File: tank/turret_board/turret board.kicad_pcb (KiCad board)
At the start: 2 copper layers, 69 x 39 mm, 22 parts, among them P1 Power, P2 IR Beacon, P3 SigIn, P4 IR Tx, P5 IR Rx, U1 LM317T, U2 pixart_ir, Y1 Crystal_4pin

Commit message: main board v0.1
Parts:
- removed ?: , Tank:MIAR
- removed P1: Power, JST:JST_EH_B02B-EH-A_02x2.50mm_Straight
- removed P2: IR Beacon, JST:JST_EH_B02B-EH-A_02x2.50mm_Straight
- removed P3: SigIn, JST:JST_EH_B04B-EH-A_04x2.50mm_Straight
- removed P4: IR Tx, JST:JST_EH_B02B-EH-A_02x2.50mm_Straight
- removed P5: IR Rx, JST:JST_EH_B03B-EH-A_03x2.50mm_Straight
- removed the REF** at (150.0, 70.0)
- removed the REF** at (209.0, 70.0)
- added Beacon1: CONN_01X02, JST:JST_EH_B02B-EH-A_02x2.50mm_Straight, F.Cu at (208.3, 64.8)
- added C5: C, Capacitors_THT:C_Disc_D3.0mm_W1.6mm_P2.50mm, F.Cu at (177.8, 86.4)
- added D1: D, Diodes_THT:D_T-1_P5.08mm_Horizontal, F.Cu at (181.6, 82.5)
- added D2: D, Diodes_THT:D_T-1_P5.08mm_Horizontal, F.Cu at (189.2, 82.5)
- added D3: D, Diodes_THT:D_T-1_P5.08mm_Horizontal, F.Cu at (185.4, 82.5)
- added G***: LOGO, modules:miar_logo, B.Cu at (182.9, 71.1)
- added J1: Conn_01x06, Connectors_JAE:JAE_LY20-06P-2T_2x03x2.00mm_Straight, F.Cu at (224.8, 96.5)
- added J2: Conn_01x06, Connectors_JAE:JAE_LY20-06P-2T_2x03x2.00mm_Straight, F.Cu at (232.4, 77.5)
- added Pwr1: CONN_01X02, JST:JST_EH_B02B-EH-A_02x2.50mm_Straight, F.Cu at (172.7, 76.2)
- added Q1: Q_NPN_BCE, Transistors_OldSowjetAera:OldSowjetaera_Transistor_Type-I_SmallPads, F.Cu at (184.2, 67.3)
- added Q2: Q_NPN_BCE, Transistors_OldSowjetAera:OldSowjetaera_Transistor_Type-I_SmallPads, F.Cu at (185.4, 92.7)
- added R8: R, Resistors_THT:R_Axial_DIN0207_L6.3mm_D2.5mm_P7.62mm_Horizontal, F.Cu at (218.4, 78.7)
- added R9: R, Resistors_THT:R_Axial_DIN0207_L6.3mm_D2.5mm_P7.62mm_Horizontal, F.Cu at (223.5, 78.7)
- added REF**: MountingHole_2.2mm_M2, Mounting_Holes:MountingHole_2.2mm_M2, F.Cu at (232.4, 72.4)
- added REF**: MountingHole_3.2mm_M3, Mounting_Holes:MountingHole_3.2mm_M3, F.Cu at (171.4, 66.0)
- added REF**: MountingHole_3.2mm_M3, Mounting_Holes:MountingHole_3.2mm_M3, F.Cu at (215.9, 94.0)
- added REF**: MountingHole_2.2mm_M2, Mounting_Holes:MountingHole_2.2mm_M2, F.Cu at (232.4, 88.9)
- added Rx1: CONN_01X03, JST:JST_EH_B03B-EH-A_03x2.50mm_Straight, F.Cu at (218.4, 64.8)
- added SigIn1: CONN_01X04, JST:JST_EH_B04B-EH-A_04x2.50mm_Straight, F.Cu at (172.7, 88.9)
- added Tx1: TX, JST:JST_EH_B02B-EH-A_02x2.50mm_Straight, F.Cu at (223.5, 83.8)
- U2: footprint pixart_ir -> modules:pixart_ir
- moved Y1 58.3 mm to (213.4, 72.4), turned to 270 degrees
- moved U2 54.0 mm to (238.8, 85.1), turned to 0 degrees
- moved U1 41.7 mm to (198.1, 94.0)
- moved R4 29.9 mm to (218.4, 81.3), turned to 270 degrees
- moved C3 29.8 mm to (194.3, 64.8), turned to 180 degrees
- moved R7 23.5 mm to (177.8, 90.2), turned to 270 degrees
- moved R1 22.6 mm to (193.0, 78.7), turned to 90 degrees
- moved C1 18.5 mm to (200.7, 64.8), turned to 180 degrees
- moved R3 17.8 mm to (200.7, 88.9)
- moved C4 16.7 mm to (185.4, 86.4)
- moved R2 16.2 mm to (193.0, 88.9)
- moved R5 15.5 mm to (196.8, 71.1), turned to 270 degrees
- moved C2 13.1 mm to (207.0, 94.0), turned to 0 degrees
- moved R6 10.5 mm to (196.8, 88.9), turned to 90 degrees
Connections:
- C1 pad 2: Net-(C1-Pad2) -> GND
- C2 pad 1: Net-(C1-Pad2) -> Net-(C1-Pad1)
- C2 pad 2: Net-(C1-Pad2) -> GND
- C3 pad 1: +3V3 -> 3.3V
- C3 pad 2: Net-(C1-Pad2) -> GND
- C4 pad 1: Net-(C4-Pad1) -> RESET
- C4 pad 2: Net-(C1-Pad2) -> GND
- R1 pad 2: Net-(C1-Pad1) -> IRSig
- R3 pad 2: Net-(C1-Pad2) -> GND
- R4 pad 1: +3V3 -> 3.3V
- R5 pad 1: +3V3 -> 3.3V
- R5 pad 2: Net-(C4-Pad1) -> RESET
- R6 pad 1: +3V3 -> SLC
- R6 pad 2: Net-(P3-Pad2) -> 3.3V
- R7 pad 1: +3V3 -> SDA
- R7 pad 2: Net-(P3-Pad1) -> 3.3V
- U1 pad 2: +3V3 -> 3.3V
- U1 pad 3: Net-(C1-Pad2) -> Net-(C1-Pad1)
- U2 pad 1: +3V3 -> Net-(J2-Pad1)
- U2 pad 2: Net-(C1-Pad2) -> Net-(J2-Pad2)
- U2 pad 3: Net-(C1-Pad2) -> Net-(J2-Pad2)
- U2 pad 5: Net-(P3-Pad1) -> Net-(J2-Pad6)
- U2 pad 6: Net-(P3-Pad2) -> Net-(J2-Pad5)
- U2 pad 7: Net-(U2-Pad7) -> Net-(J2-Pad4)
- U2 pad 8: Net-(C4-Pad1) -> Net-(J2-Pad3)
- Y1 pad 14: Net-(C1-Pad1) -> 5V
- Y1 pad 7: Net-(C1-Pad2) -> GND
- Y1 pad 8: Net-(U2-Pad7) -> Net-(J1-Pad4)
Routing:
- net GND: track 0.00 -> 151.4 mm, vias 0 -> 1
- net Net-(C1-Pad2): track 127.5 -> 0.00 mm
- net 3.3V: track 0.00 -> 100.7 mm
- net Net-(Rx1-Pad3): track 0.00 -> 81.3 mm, vias 0 -> 1
- net +3V3: track 75.7 -> 0.00 mm, vias 2 -> 0
- net Beacon: track 0.00 -> 75.6 mm
- net Net-(P3-Pad1): track 69.6 -> 0.00 mm, vias 1 -> 0
- net Net-(D2-Pad1): track 0.00 -> 65.2 mm, vias 0 -> 1
- net SLC: track 0.00 -> 60.5 mm, vias 0 -> 1
- net SDA: track 0.00 -> 57.7 mm, vias 0 -> 1
- net Net-(P3-Pad2): track 50.8 -> 0.00 mm, vias 2 -> 0
- net RESET: track 0.00 -> 50.7 mm, vias 0 -> 1
- net IRSig: track 0.00 -> 38.7 mm
- net Net-(C4-Pad1): track 38.0 -> 0.00 mm
- net Net-(J2-Pad3): track 0.00 -> 33.8 mm
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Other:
- board size 69 x 39 mm -> 80 x 44.4 mm
- board text added: "Turret Board v0.3 Laser Tag Robot Tank M.I.A.R. Labs nick.groesz@gmail.com"
- board text removed: "Turret Board v0.2 Laser Bot M.I.A.R. Labs"

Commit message: interim
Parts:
- removed C2, C4: C, Capacitors_THT:C_Disc_D3.0mm_W1.6mm_P2.50mm
- removed G***: LOGO, modules:miar_logo
- removed Pwr1: CONN_01X02, JST:JST_EH_B02B-EH-A_02x2.50mm_Straight
- removed R1, R3, R4: R, Resistors_THT:R_Axial_DIN0207_L6.3mm_D2.5mm_P7.62mm_Horizontal
- removed the REF** at (232.4, 72.4)
- removed the REF** at (171.4, 66.0)
- removed the REF** at (215.9, 94.0)
- removed the REF** at (232.4, 88.9)
- added J3: Conn_01x02_Male, JST:JST_EH_B02B-EH-A_02x2.50mm_Straight, F.Cu at (186.7, 117.5)
- added REF**: MountingHole_2.2mm_M2, Mounting_Holes:MountingHole_2.2mm_M2, F.Cu at (186.7, 96.5)
- added REF**: MountingHole_2.2mm_M2, Mounting_Holes:MountingHole_2.2mm_M2, F.Cu at (187.3, 123.2)
- added REF**: MountingHole_2.2mm_M2, Mounting_Holes:MountingHole_2.2mm_M2, F.Cu at (222.2, 96.5)
- added REF**: MountingHole_2.2mm_M2, Mounting_Holes:MountingHole_2.2mm_M2, F.Cu at (222.2, 123.2)
- J1, J2: footprint Connectors_JAE:JAE_LY20-06P-2T_2x03x2.00mm_Straight -> Pin_Headers:Pin_Header_Straight_2x03_Pitch2.54mm
- Q1, Q2: value Q_NPN_BCE -> 2N3904; footprint Transistors_OldSowjetAera:OldSowjetaera_Transistor_Type-I_SmallPads -> TO_SOT_Packages_THT:TO-92_Inline_Narrow_Oval
- U1: value LM317T -> KA378R33; footprint Tank:LM317T -> TO_SOT_Packages_THT:TO-220-4_Vertical
- moved C1 59.0 mm to (192.4, 123.2), turned to 90 degrees
- moved R5 57.5 mm to (218.4, 124.5), turned to 90 degrees
- moved Q1 56.8 mm to (209.6, 118.1)
- moved C3 52.1 mm to (192.4, 116.8), turned to 90 degrees
- moved R8 50.0 mm to (196.8, 123.8)
- moved R7 44.1 mm to (206.4, 123.8), turned to 90 degrees
- moved R9 42.6 mm to (203.2, 116.2), turned to 270 degrees
- moved R2 41.9 mm to (215.3, 124.5)
- moved Q2 39.4 mm to (209.6, 123.8), turned to 0 degrees
- moved C5 36.0 mm to (201.3, 113.7), turned to 180 degrees
- moved R6 35.1 mm to (200.0, 123.8)
- moved D1 34.3 mm to (200.7, 111.1)
- moved Y1 33.8 mm to (203.8, 104.8), turned to 0 degrees
- moved Rx1 33.5 mm to (207.6, 96.5), turned to 180 degrees
- moved Beacon1 31.6 mm to (214.0, 95.9)
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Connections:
- D2 pad 2: Net-(D2-Pad2) -> IRSig
- D3 pad 2: Net-(D2-Pad2) -> IRSig
- J1 pad 3: RESET -> GND
- Q1 pad 1: Net-(D3-Pad1) -> GND
- Q1 pad 2: Net-(D2-Pad1) -> Net-(D3-Pad1)
- Q1 pad 3: GND -> Net-(D2-Pad1)
- Q2 pad 1: Net-(Q2-Pad1) -> GND
- Q2 pad 2: Beacon -> Net-(Q2-Pad2)
- Q2 pad 3: GND -> Beacon
- R2 pad 1: Net-(Q2-Pad1) -> Net-(Q2-Pad2)
- R5 pad 2: RESET -> GND
- Rx1 pad 3: Net-(Rx1-Pad3) -> IRRx
- SigIn1 pad 3: Net-(Rx1-Pad3) -> IRSig
- SigIn1 pad 4: IRSig -> IRRx
- U1 pad 1: Net-(R3-Pad1) -> Net-(C1-Pad1)
- U1 pad 3: Net-(C1-Pad1) -> GND
- Y1 pad 14: 5V -> 3.3V
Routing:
- net GND: track 151.4 -> 0.00 mm, vias 1 -> 0
- net 3.3V: track 100.7 -> 0.00 mm
- net Net-(Rx1-Pad3): track 81.3 -> 0.00 mm, vias 1 -> 0
- net Beacon: track 75.6 -> 0.00 mm
- net Net-(C1-Pad1): track 73.5 -> 0.00 mm, vias 1 -> 0
- net Net-(D2-Pad1): track 65.2 -> 0.00 mm, vias 1 -> 0
- net SLC: track 60.5 -> 0.00 mm, vias 1 -> 0
- net SDA: track 57.7 -> 0.00 mm, vias 1 -> 0
- net RESET: track 50.7 -> 0.00 mm, vias 1 -> 0
- net IRSig: track 38.7 -> 0.00 mm
- net Net-(J2-Pad3): track 33.8 -> 0.00 mm
- net 5V: track 27.6 -> 0.00 mm
- net Net-(R3-Pad1): track 23.9 -> 0.00 mm
- net Net-(D3-Pad1): track 22.4 -> 0.00 mm
- net Net-(J2-Pad2): track 20.5 -> 0.00 mm
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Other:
- board size 80 x 44.4 mm -> 44.4 x 34.3 mm
- board text removed: "Turret Board v0.3 Laser Tag Robot Tank M.I.A.R. Labs nick.groesz@gmail.com"

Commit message: Turret Board v0.4
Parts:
- added G***: LOGO, modules:Tank, B.Cu at (211.5, 116.8)
- added REF**: MountingHole_2.2mm_M2, Mounting_Holes:MountingHole_2.2mm_M2, F.Cu at (241.3, 117.5)
- added REF**: MountingHole_2.2mm_M2, Mounting_Holes:MountingHole_2.2mm_M2, F.Cu at (231.8, 116.8)
- added REF**: MountingHole_2.2mm_M2, Mounting_Holes:MountingHole_2.2mm_M2, F.Cu at (231.8, 102.2)
- added REF**: MountingHole_2.2mm_M2, Mounting_Holes:MountingHole_2.2mm_M2, F.Cu at (241.3, 101.6)
- moved U1 26.4 mm to (207.6, 123.8)
- moved R7 20.7 mm to (192.4, 108.6)
- moved R8 15.4 mm to (198.8, 108.6)
- moved Q2 14.5 mm to (203.8, 110.5), turned to 90 degrees
- moved Q1 14.5 mm to (203.8, 104.8), turned to 90 degrees
- moved Y1 13.9 mm to (217.2, 101.0), turned to 270 degrees
- moved R9 10.8 mm to (195.6, 108.6), turned to 90 degrees
- moved D3 10.5 mm to (204.5, 113.7), turned to 270 degrees
- moved R6 9.53 mm to (192.4, 118.1)
- moved SigIn1 7.01 mm to (187.3, 101.6), turned to 270 degrees
- moved C1 6.48 mm to (198.8, 121.9), turned to 270 degrees
- moved R5 5.24 mm to (217.2, 119.4), turned to 0 degrees
- moved C3 5.12 mm to (193.0, 121.9), turned to 270 degrees
- moved R2 5.08 mm to (215.3, 119.4), turned to 180 degrees
- moved D1 4.58 mm to (196.8, 113.7), turned to 270 degrees
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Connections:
- C1 pad 1: Net-(C1-Pad1) -> 5V
- J1 pad 3: GND -> RESET
- J3 pad 1: Net-(C1-Pad1) -> 5V
- R5 pad 2: GND -> RESET
- U1 pad 1: Net-(C1-Pad1) -> 5V
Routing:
- net GND: track 0.00 -> 119.0 mm
- net 5V: track 0.00 -> 93.2 mm
- net 3.3V: track 0.00 -> 82.6 mm, vias 0 -> 1
- net SLC: track 0.00 -> 56.0 mm
- net SDA: track 0.00 -> 43.5 mm
- net IRRx: track 0.00 -> 34.3 mm
- net Beacon: track 0.00 -> 33.3 mm
- net IRSig: track 0.00 -> 29.9 mm
- net Net-(J2-Pad1): track 0.00 -> 22.1 mm
- net Net-(Q2-Pad2): track 0.00 -> 21.6 mm, vias 0 -> 1
- net Net-(D2-Pad1): track 0.00 -> 19.5 mm
- net Net-(J2-Pad2): track 0.00 -> 19.4 mm
- net Net-(C5-Pad1): track 0.00 -> 17.0 mm
- net Net-(J1-Pad4): track 0.00 -> 16.5 mm
- net IRTx: track 0.00 -> 14.2 mm
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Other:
- board size 44.4 x 34.3 mm -> 59.7 x 32.4 mm
- board text added: "Turret Board v0.4 Laser Tag Robot Tank M.I.A.R. Labs nick.groesz@gmail.com"

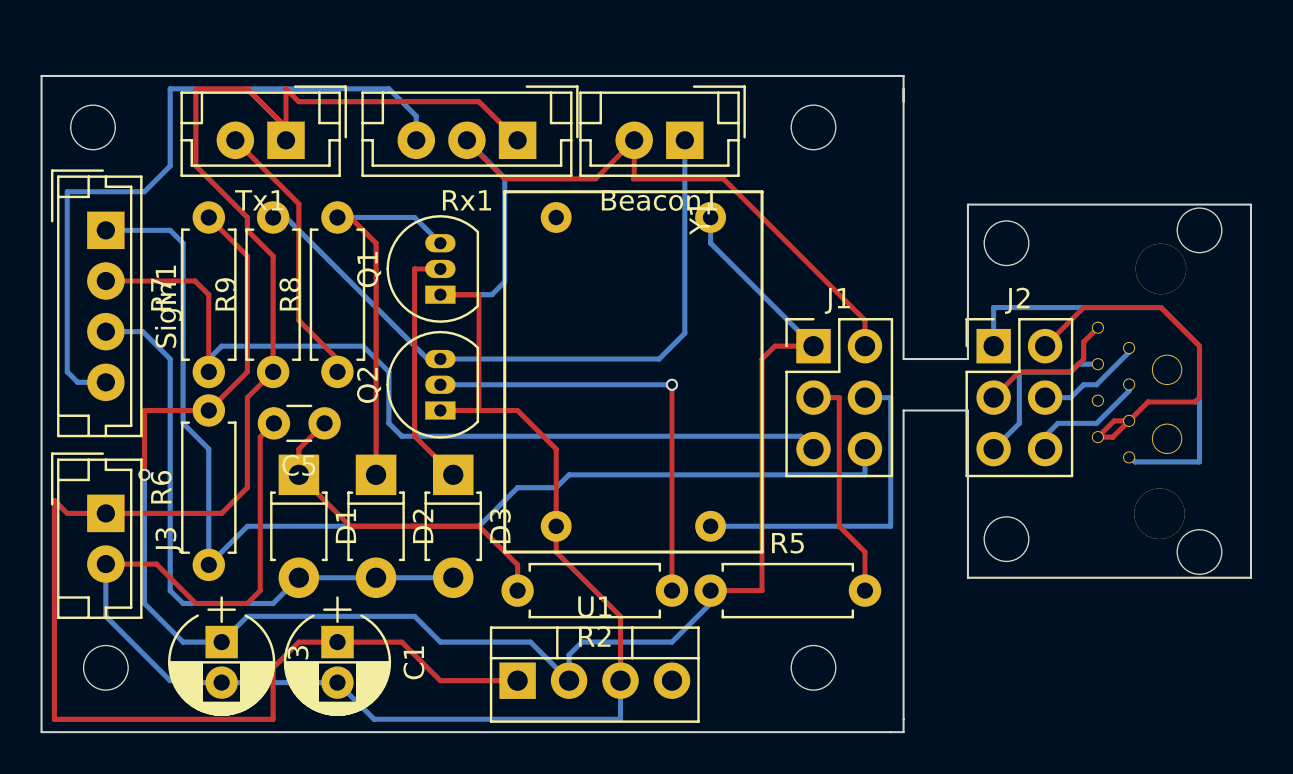
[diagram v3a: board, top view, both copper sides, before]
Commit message: Turret board version 0.5: - camera is integrated onto board
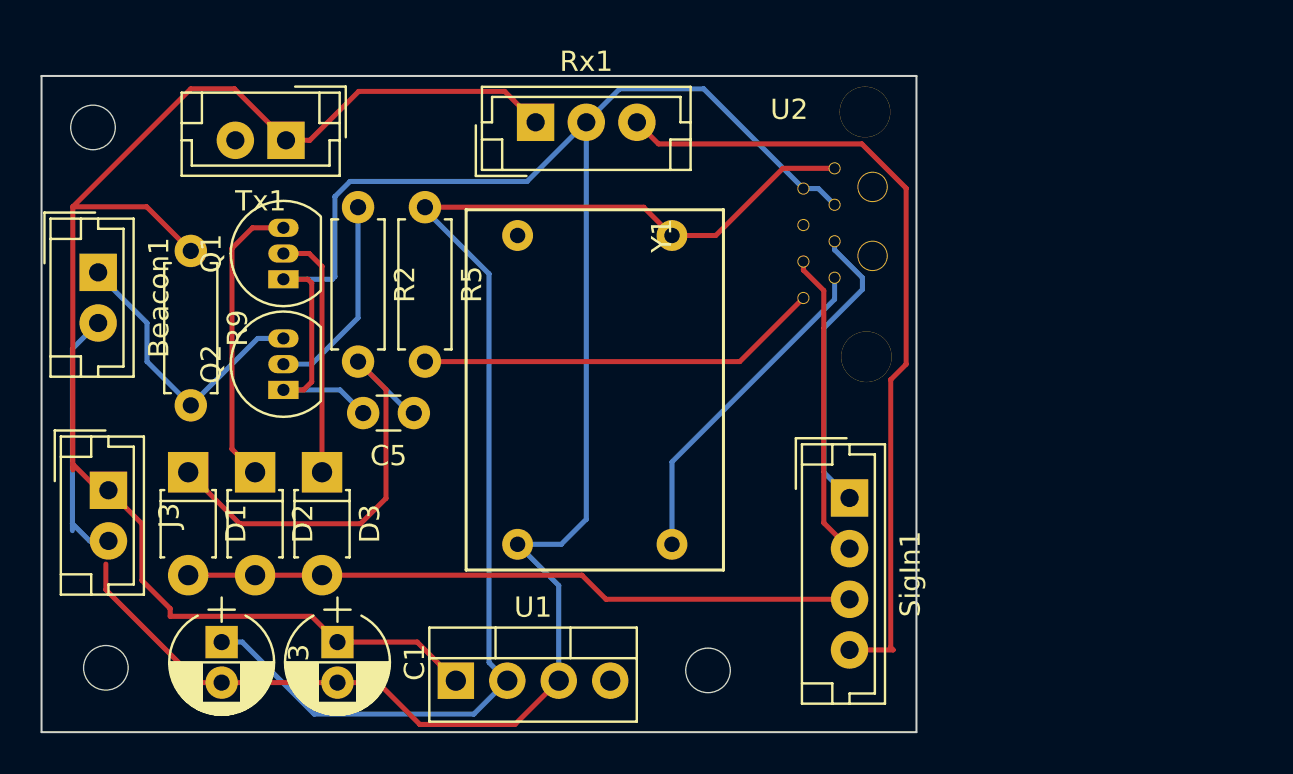
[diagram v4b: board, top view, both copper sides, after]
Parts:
- removed J1, J2: Conn_01x06, Pin_Headers:Pin_Header_Straight_2x03_Pitch2.54mm
- removed R6, R7, R8: R, Resistors_THT:R_Axial_DIN0207_L6.3mm_D2.5mm_P7.62mm_Horizontal
- removed the REF** at (241.3, 117.5)
- removed the REF** at (231.8, 116.8)
- removed the REF** at (231.8, 102.2)
- removed the REF** at (222.2, 123.2)
- removed the REF** at (241.3, 101.6)
- U2: moved to F.Cu
- moved SigIn1 39.0 mm to (224.0, 114.8)
- moved Beacon1 29.7 mm to (186.9, 103.7), turned to 270 degrees
- moved REF** 27.3 mm to (217.0, 123.3)
- moved U2 25.6 mm to (221.1, 95.1)
- moved R2 24.5 mm to (199.8, 100.5), turned to 270 degrees
- moved R5 23.6 mm to (203.1, 100.5), turned to 270 degrees
- moved Q2 7.81 mm to (196.1, 109.5)
- moved Q1 7.78 mm to (196.1, 104.0)
- moved R9 7.22 mm to (191.5, 102.6), turned to 270 degrees
- moved D3 6.48 mm to (198.0, 113.5)
- moved D2 5.97 mm to (194.7, 113.5)
- moved D1 5.46 mm to (191.4, 113.5)
- moved C5 4.43 mm to (202.5, 110.6)
- moved U1 3.05 mm to (204.6, 123.8)
- moved Y1 2.10 mm to (215.3, 101.9)
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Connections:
- U2 pad 1: Net-(J2-Pad1) -> 3.3V
- U2 pad 2: Net-(J2-Pad2) -> GND
- U2 pad 3: Net-(J2-Pad2) -> GND
- U2 pad 5: Net-(J2-Pad6) -> SLC
- U2 pad 6: Net-(J2-Pad5) -> SDA
- U2 pad 7: Net-(J2-Pad4) -> Net-(U2-Pad7)
- U2 pad 8: Net-(J2-Pad3) -> RESET
- Y1 pad 8: Net-(J1-Pad4) -> Net-(U2-Pad7)
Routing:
- net SLC: track 56.0 -> 14.6 mm
- net SDA: track 43.5 -> 15.1 mm
- net Net-(J2-Pad1): track 22.1 -> 0.00 mm
- net 5V: track 93.2 -> 72.8 mm
- net Net-(J2-Pad2): track 19.4 -> 0.00 mm
- net 3.3V: track 82.6 -> 63.7 mm, vias 1 -> 0
- net Beacon: track 33.3 -> 14.4 mm
- net Net-(J1-Pad4): track 16.5 -> 0.00 mm
- net Net-(U2-Pad7): track 0.00 -> 16.5 mm
- net IRTx: track 14.2 -> 0.00 mm
- net Net-(Q2-Pad2): track 21.6 -> 10.1 mm, vias 1 -> 0
- net RESET: track 11.3 -> 20.1 mm
- net Net-(J2-Pad5): track 8.37 -> 0.00 mm
- net Net-(J2-Pad3): track 7.07 -> 0.00 mm
- net Net-(J2-Pad6): track 6.02 -> 0.00 mm
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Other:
- board size 59.7 x 32.4 mm -> 43.2 x 32.4 mm
- board text added: "Turret Board v0.5 Laser Tag Robot Tank M.I.A.R. Labs nick.groesz@gmail.com"
- board text removed: "Turret Board v0.4 Laser Tag Robot Tank M.I.A.R. Labs nick.groesz@gmail.com"

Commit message: turret board interim
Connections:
- J3 pad 1: 5V -> Net-(C1-Pad1)
- U1 pad 1: 5V -> Net-(C1-Pad1)
